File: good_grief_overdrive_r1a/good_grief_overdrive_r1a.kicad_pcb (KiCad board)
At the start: 2 copper layers, 86.4 x 95.3 mm, 69 parts, among them J1 0.6, J2 0.5, J3 0.5, X1 +, X2 -, X3 COM, X4 COM

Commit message: Good Grief Overdrive [REV1]: minor changes
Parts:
- HL1, HL2: footprint KCL:LED-ROUND-05.0-UNI-SH-SPACER -> KCL:LED-ROUND-05.0-UNI-SH-SPACER-PNL-5.3
- SB1: footprint KCL:SW-PBS-24-302SP-small -> SBKCL:SW-PBS-24-302SP-2.5

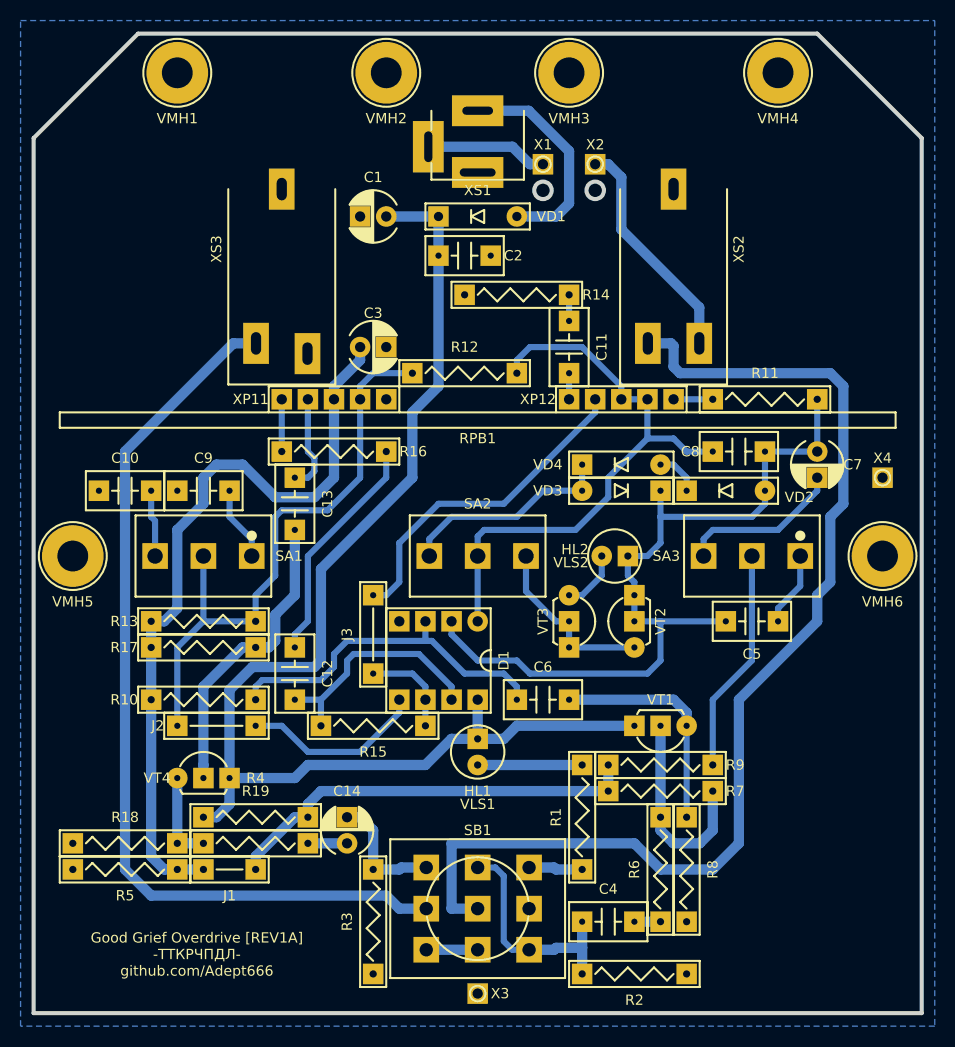
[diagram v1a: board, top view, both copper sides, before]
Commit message: Good Grief Overdrive [REV1]: many footprints replaced with single-layer footprints
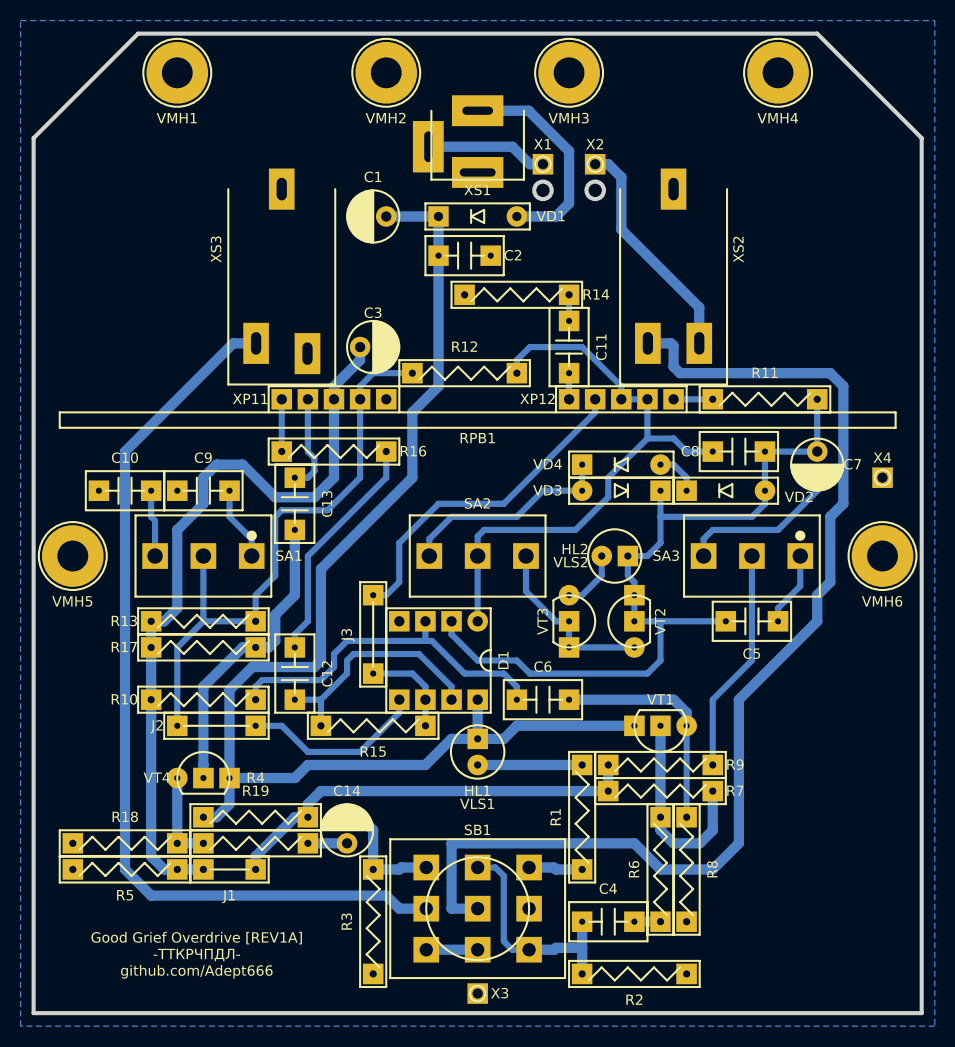
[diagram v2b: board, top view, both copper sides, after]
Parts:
- C1, C14, C3, C7: footprint KCL:CP-RADIAL-D05.0-P02.0-CLS -> KCL-TH-SL:CP-RADIAL-D05.0-P02.0-CLS
- C10, C11, C12, C13, C2, C4, C5, C6, C8, C9: footprint KCL:C-DISK-D04.2-T03.0-P05.08-d0.5 -> KCL-TH-SL:C-DISK-D04.2-T03.0-P05.08-d0.5
- D1: footprint KCL:P-DIP-08 -> KCL-TH-SL:P-DIP-08
- GB1: footprint KCL:B-PP3-HV -> KCL-VIRTUAL:B-PP3-HV
- HL1, HL2: footprint KCL:LED-ROUND-05.0-UNI-SH-SPACER-PNL-5.3 -> KCL-TH-SL:LED-ROUND-05.0-UNI-SH-SPACER-PNL-5.3
- J1: footprint KCL:J-TH-d0.6-P05.08 -> KCL-TH-SL:J-TH-d0.6-P05.08
- J2, J3: footprint KCL:J-TH-d0.5-P07.62 -> KCL-TH-SL:J-TH-d0.5-P07.62
- R1, R10, R11, R12, R13, R14, R15, R16, R17, R18, R19, R2, R3, R4, R5, R6, R7, R8, R9: footprint KCL:R-MFR-25 -> KCL-TH-SL:R-MFR-25
- SA1, SA3: footprint SBKCL:SW-MTS-102-A2-2.5 -> KCL-TH-SL:SW-MTS-102-A2-2.5-PNL-6.4
- SA2: footprint SBKCL:SW-MTS-103-A2-2.5 -> KCL-TH-SL:SW-MTS-103-A2-2.5-PNL-6.4
- SB1: footprint SBKCL:SW-PBS-24-302SP-2.5 -> KCL-TH-SL:SW-PBS-24-302SP-2.5-PNL-13.0
- VD1: footprint KCL:P-DO-41 -> KCL-TH-SL:P-DO-41
- VD2, VD3, VD4: footprint KCL:P-DO-35 -> KCL-TH-SL:P-DO-35
- VLS1, VLS2: footprint KCL:VLS-BR -> KCL-VIRTUAL:VLS-BR
- VT1, VT4: footprint KCL:P-TO-92-E-B-C -> KCL-TH-SL:P-TO-92-E-B-C
- VT2, VT3: footprint KCL:P-TO-92-S-G-D -> KCL-TH-SL:P-TO-92-S-G-D
- X1, X2, X3, X4: footprint KCL:CON-PAD-S-1.0-2.0 -> KCL-TH-SL:CON-PAD-S-1.0-2.0
- XS1: footprint KCL:CON-DC-005 -> KCL-TH-SL:CON-DC-005

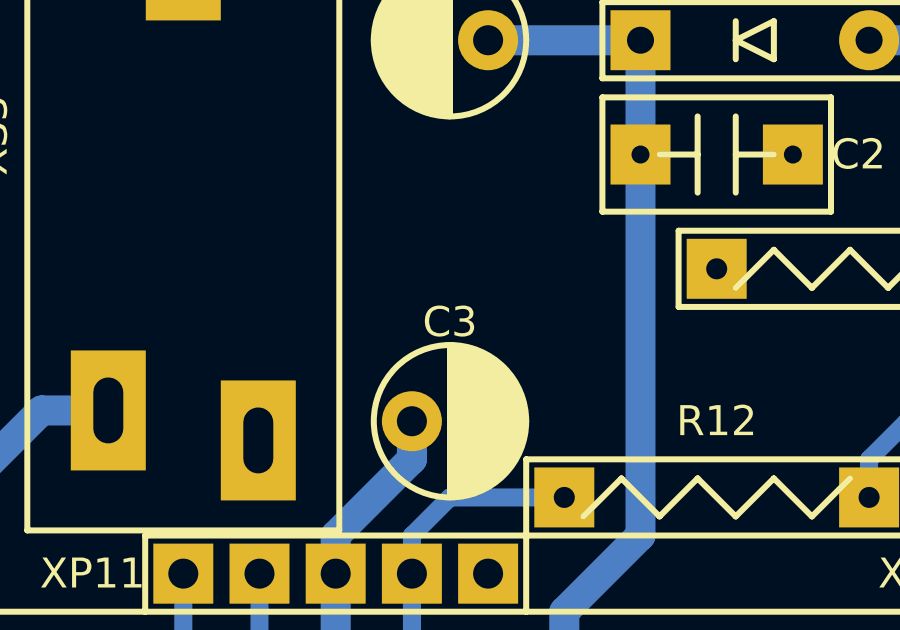
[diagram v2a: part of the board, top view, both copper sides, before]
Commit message: Good Grief Overdrive [REV1]: all remaining footprints replaced with single-layer footprints
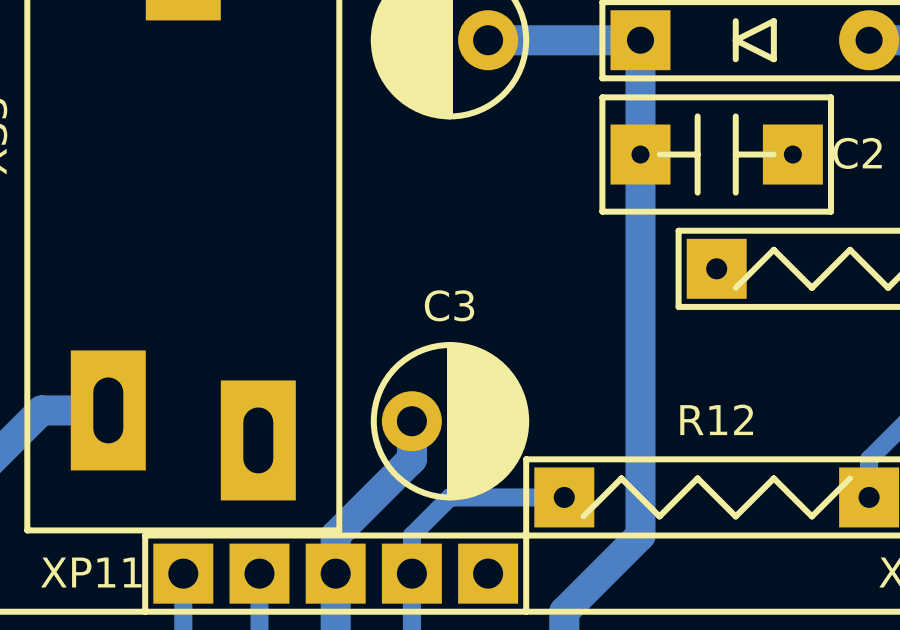
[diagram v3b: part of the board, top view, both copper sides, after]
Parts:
- RPB1: footprint SBKCL:RPB-18-3x17 -> SBKCL-TH-SL:RPB-1590BB-18-3x17-1.5-PNL-7.4-2.6
- VMH1, VMH2, VMH3, VMH4, VMH5, VMH6: footprint KCL:VMH-STA-DA5 -> KCL-TH-SL:VMH-STA-DA5-PNL-3.0
- XS2: footprint KCL:CON-ST-008X-04 -> KCL-TH-SL:CON-ST-008X-04
- XS3: footprint KCL:CON-ST-008X-05 -> KCL-TH-SL:CON-ST-008X-05

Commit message: Good Grief Overdrive [REV1]: silkscreen edited
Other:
- board text added: "+"
- board text added: "-"
- board text added: "GOOD GRIEF OVERDRIVE [REV1A] -ТТКРЧПДЛ- GITHUB.COM/ADEPT666"
- board text removed: "Good Grief Overdrive [REV1A] -ТТКРЧПДЛ- github.com/Adept666"

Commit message: Good Grief Overdrive [REV1]: minor changes
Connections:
- net /IN-SCH renamed /IN-CIR
- net /OUT-SCH renamed /OUT-CIR
